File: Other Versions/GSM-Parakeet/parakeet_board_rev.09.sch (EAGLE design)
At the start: 14 parts

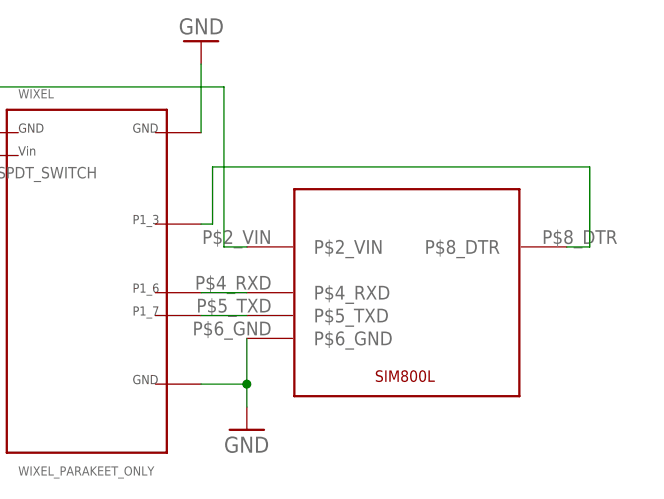
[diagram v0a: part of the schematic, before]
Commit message: Updated Parakeet rev.09
Fixed SIM800 module dimensions
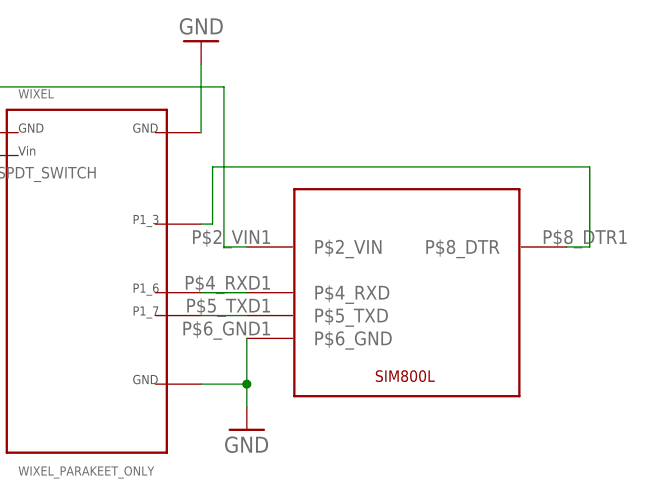
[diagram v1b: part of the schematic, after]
